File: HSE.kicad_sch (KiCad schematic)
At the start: 5 parts, among them Y2 25MHz

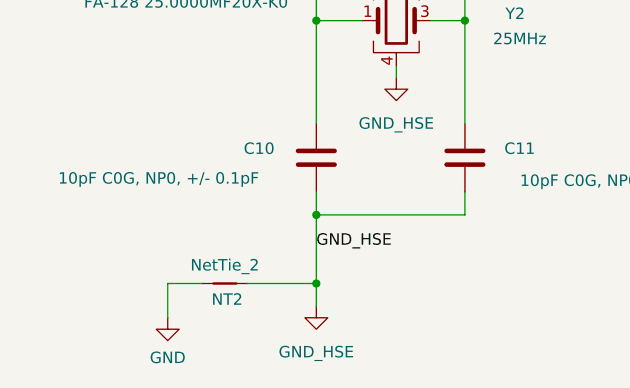
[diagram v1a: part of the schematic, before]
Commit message: added footprint and step model. Cleaned up silkscreen and fab layers.
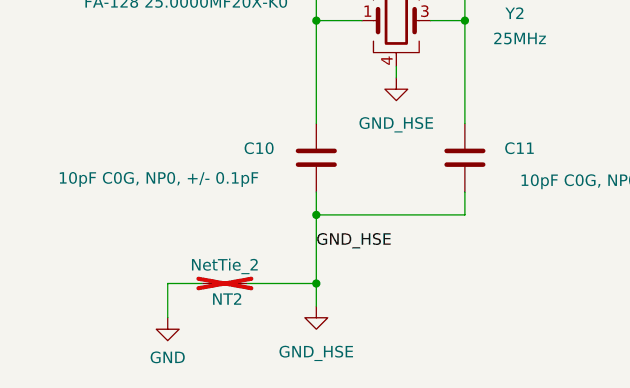
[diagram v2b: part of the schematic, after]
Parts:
- NT2: now not fitted
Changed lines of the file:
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@@
 		(in_bom no)
 		(on_board yes)
-		(dnp no)
+		(dnp yes)
 		(property "Reference" "NT2"
 			(at 128.524 124.968 0)
